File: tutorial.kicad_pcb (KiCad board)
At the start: 2 copper layers, 175 x 164.8 mm, 68 parts

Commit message: define pins
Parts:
- removed the _1 at (246.1, 152.0) (x2)
- added _1 (x2): RPi_Pico_SMD_TH, RPi_Pico_SMD_TH, F.Cu at (246.1, 152.0)
- moved B1 13.9 mm to (229.8, 185.4)
- moved B2 13.9 mm to (229.8, 185.4)
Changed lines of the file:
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@@
         (descr "Low-profile SMD Tactile Switch, https://www.e-switch.com/product-catalog/tact/product-lines/tl3342-series-low-profile-smt-tact-switch")
         (tags "SPST Tactile Switch")
-        (at 243.6963463 183.9408894 -15)
+        (at 229.84521529999998 185.405871 -15)
         (fp_text reference "B1" (at 0 0) (layer F.SilkS) hide (effects (font (size 1.27 1.27) (thickness 0.15))))
         (fp_text value "" (at 0 0) (layer F.SilkS) hide (effects (font (size 1.27 1.27) (thickness 0.15))))
@@
         (descr "Low-profile SMD Tactile Switch, https://www.e-switch.com/product-catalog/tact/product-lines/tl3342-series-low-profile-smt-tact-switch")
         (tags "SPST Tactile Switch")
-        (at 243.6963463 183.9408894 -15)
+        (at 229.84521529999998 185.405871 -15)
         (fp_text reference "B2" (at 0 0) (layer F.SilkS) hide (effects (font (size 1.27 1.27) (thickness 0.15))))
         (fp_text value "" (at 0 0) (layer F.SilkS) hide (effects (font (size 1.27 1.27) (thickness 0.15))))

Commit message: ready to start routing
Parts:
- removed the _1 at (246.1, 152.0) (x2)
- added ROT1: , rotary_encoder, F.Cu at (130.6, 92.3)
- added _1 (x2): RPi_Pico_SMD_TH, RPi_Pico_SMD_TH, F.Cu at (246.6, 153.1)
- added _2: , MountingHole_2.2mm_M2_Pad_Via, F.Cu at (243.6, 200.5)
- added _3: , MountingHole_2.2mm_M2_Pad_Via, F.Cu at (186.1, 203.0)
- added _4: , MountingHole_2.2mm_M2_Pad_Via, F.Cu at (197.3, 91.3)
- added _5: , MountingHole_2.2mm_M2_Pad_Via, F.Cu at (143.0, 84.7)
- moved B1 2.83 mm to (229.3, 188.2), turned to -16 degrees
- moved B2 2.83 mm to (229.3, 188.2), turned to -16 degrees
- moved TRRS1 2.06 mm to (250.4, 194.2), turned to -106 degrees
- moved S28 1.42 mm to (230.1, 120.2), turned to -16 degrees
- moved D28 1.34 mm to (228.7, 125.0), turned to -16 degrees
- moved S27 1.11 mm to (224.7, 138.7), turned to -16 degrees
- moved OLED1 1.11 mm to (244.8, 181.2), turned to -106 degrees
- moved D27 1.04 mm to (223.4, 143.5), turned to -16 degrees
- moved D31 0.95 mm to (221.7, 221.5), turned to -31 degrees
- moved S31 0.93 mm to (224.2, 217.2), turned to -31 degrees
- moved S26 0.83 mm to (219.4, 157.3), turned to -16 degrees
- moved D26 0.76 mm to (218.0, 162.1), turned to -16 degrees
- moved S24 0.75 mm to (211.5, 112.4), turned to -15.5 degrees
- moved S19 0.72 mm to (193.6, 104.8), turned to -15.5 degrees
- moved D24 0.71 mm to (210.1, 117.2), turned to -15.5 degrees
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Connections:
- OLED1 pad 3: GP5 -> GP3
- OLED1 pad 4: GP4 -> GP2
- TRRS1 pad 3: P2 -> GP15
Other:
- board size 175 x 164.8 mm -> 178.2 x 165.7 mm

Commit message: attempt to set up routing
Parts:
- removed the _1 at (246.6, 153.1) (x2)
- added _1 (x2): RPi_Pico_SMD_TH, RPi_Pico_SMD_TH, F.Cu at (246.6, 153.1)
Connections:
- D1 pad 1: (no net) -> GP12
- D10 pad 1: (no net) -> GP13
- D11 pad 1: (no net) -> GP12
- D12 pad 1: (no net) -> GP11
- D13 pad 1: (no net) -> GP10
- D14 pad 1: (no net) -> GP9
- D15 pad 1: (no net) -> GP13
- D16 pad 1: (no net) -> GP12
- D17 pad 1: (no net) -> GP11
- D18 pad 1: (no net) -> GP10
- D19 pad 1: (no net) -> GP9
- D2 pad 1: (no net) -> GP11
- D20 pad 1: (no net) -> GP13
- D21 pad 1: (no net) -> GP12
- D22 pad 1: (no net) -> GP11
- D23 pad 1: (no net) -> GP10
- D24 pad 1: (no net) -> GP9
- D25 pad 1: (no net) -> GP12
- D26 pad 1: (no net) -> GP11
- D27 pad 1: (no net) -> GP10
- D28 pad 1: (no net) -> GP9
- D29 pad 1: (no net) -> GP14
- D3 pad 1: (no net) -> GP10
- D30 pad 1: (no net) -> GP14
- D31 pad 1: (no net) -> GP14
- D4 pad 1: (no net) -> GP9
- D5 pad 1: (no net) -> GP13
- D6 pad 1: (no net) -> GP12
- D7 pad 1: (no net) -> GP11
- D8 pad 1: (no net) -> GP10
- D9 pad 1: (no net) -> GP9
- ROT1 pad 1: GP0 -> GP1
- ROT1 pad 2: GP1 -> GP9
- S1 pad 1: (no net) -> GP1
- S10 pad 1: (no net) -> GP5
- S11 pad 1: (no net) -> GP5
- S12 pad 1: (no net) -> GP5
- S13 pad 1: (no net) -> GP5
- S14 pad 1: (no net) -> GP5
- S15 pad 1: (no net) -> GP6
- S16 pad 1: (no net) -> GP6
- S17 pad 1: (no net) -> GP6
- S18 pad 1: (no net) -> GP6
- S19 pad 1: (no net) -> GP6
- S2 pad 1: (no net) -> GP1
- S20 pad 1: (no net) -> GP7
- S21 pad 1: (no net) -> GP7
- S22 pad 1: (no net) -> GP7
- S23 pad 1: (no net) -> GP7
- S24 pad 1: (no net) -> GP7
- S25 pad 1: (no net) -> GP8
- S26 pad 1: (no net) -> GP8
- S27 pad 1: (no net) -> GP8
- S28 pad 1: (no net) -> GP8
- S29 pad 1: (no net) -> GP8
- S3 pad 1: (no net) -> GP1
- S30 pad 1: (no net) -> GP8
- S31 pad 1: (no net) -> GP8
- S4 pad 1: (no net) -> GP1
- S5 pad 1: (no net) -> GP4
- S6 pad 1: (no net) -> GP4
- S7 pad 1: (no net) -> GP4
- S8 pad 1: (no net) -> GP4
- S9 pad 1: (no net) -> GP4

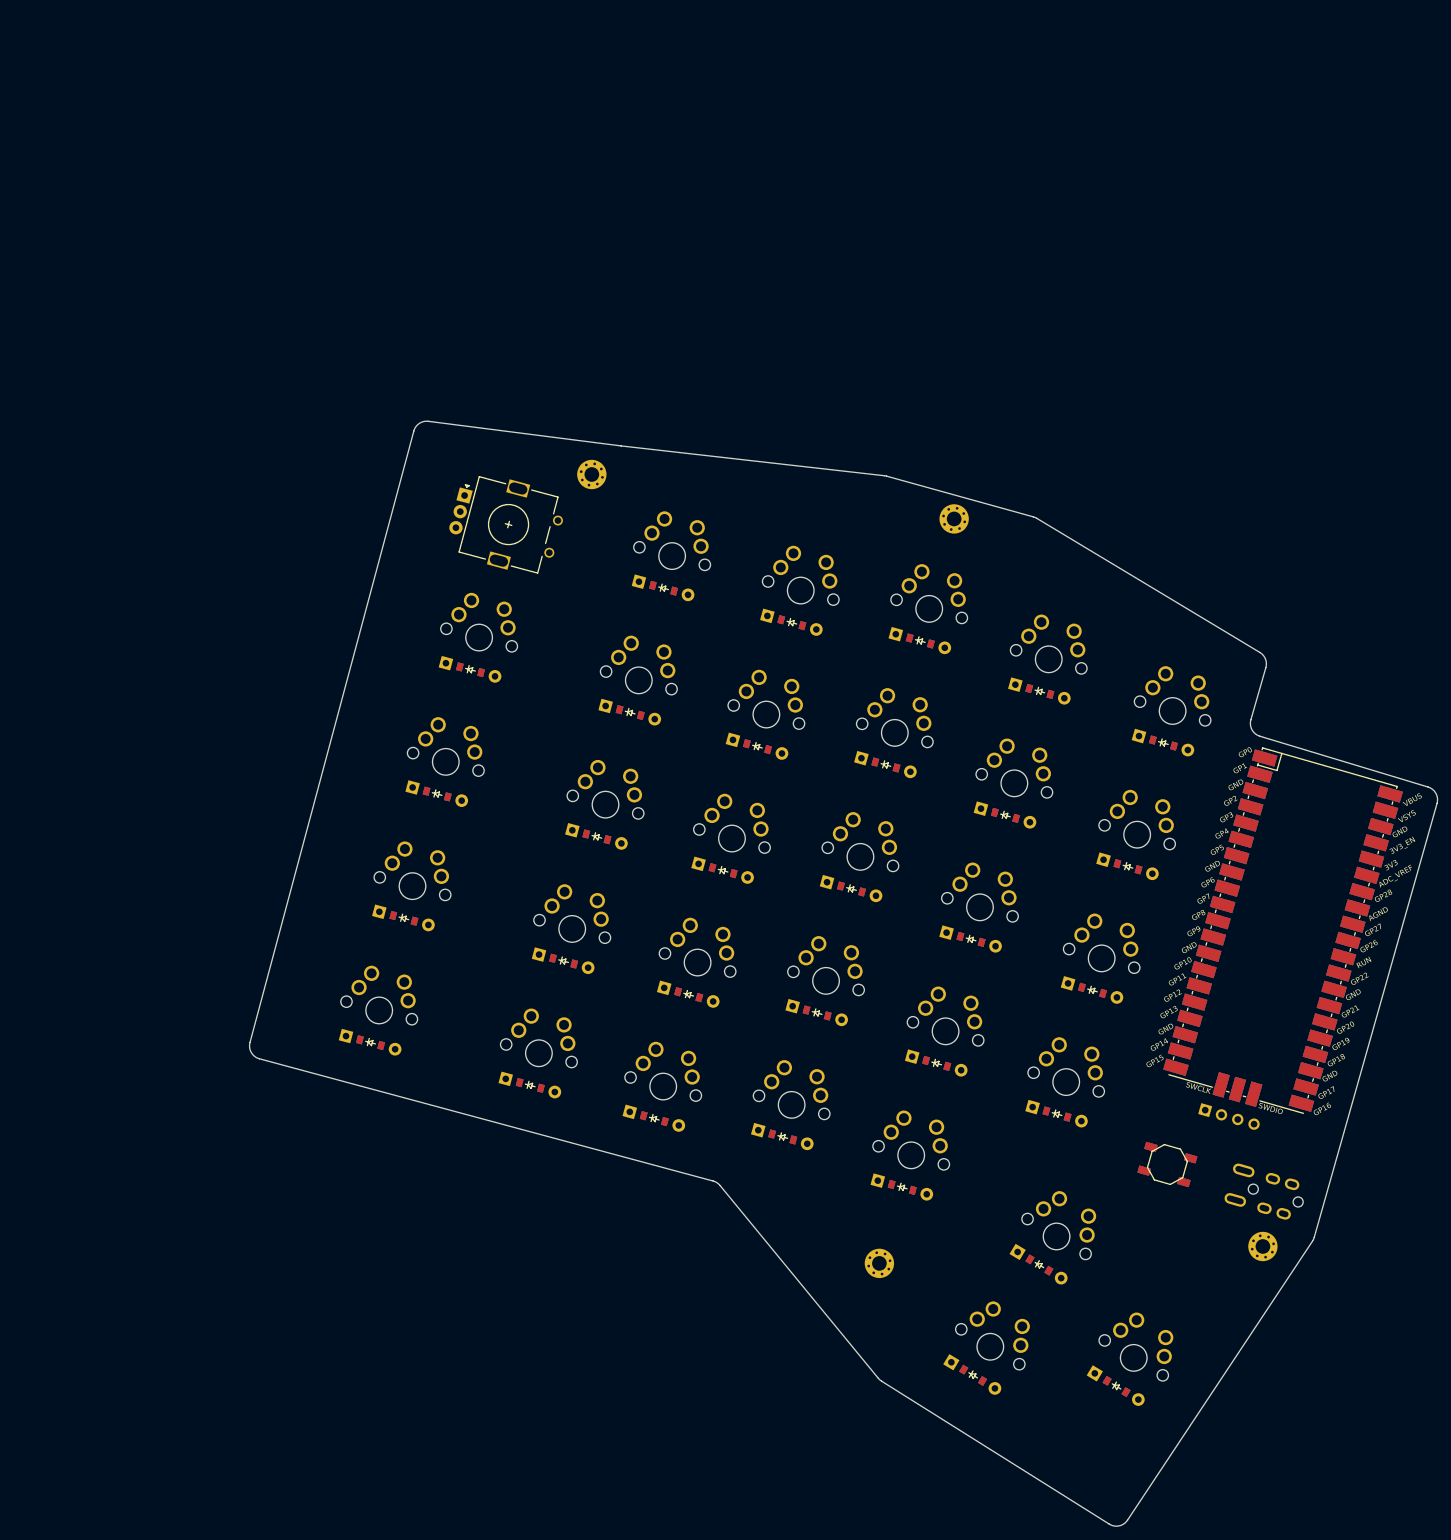
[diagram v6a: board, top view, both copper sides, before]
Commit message: routing setup done, now to actually route
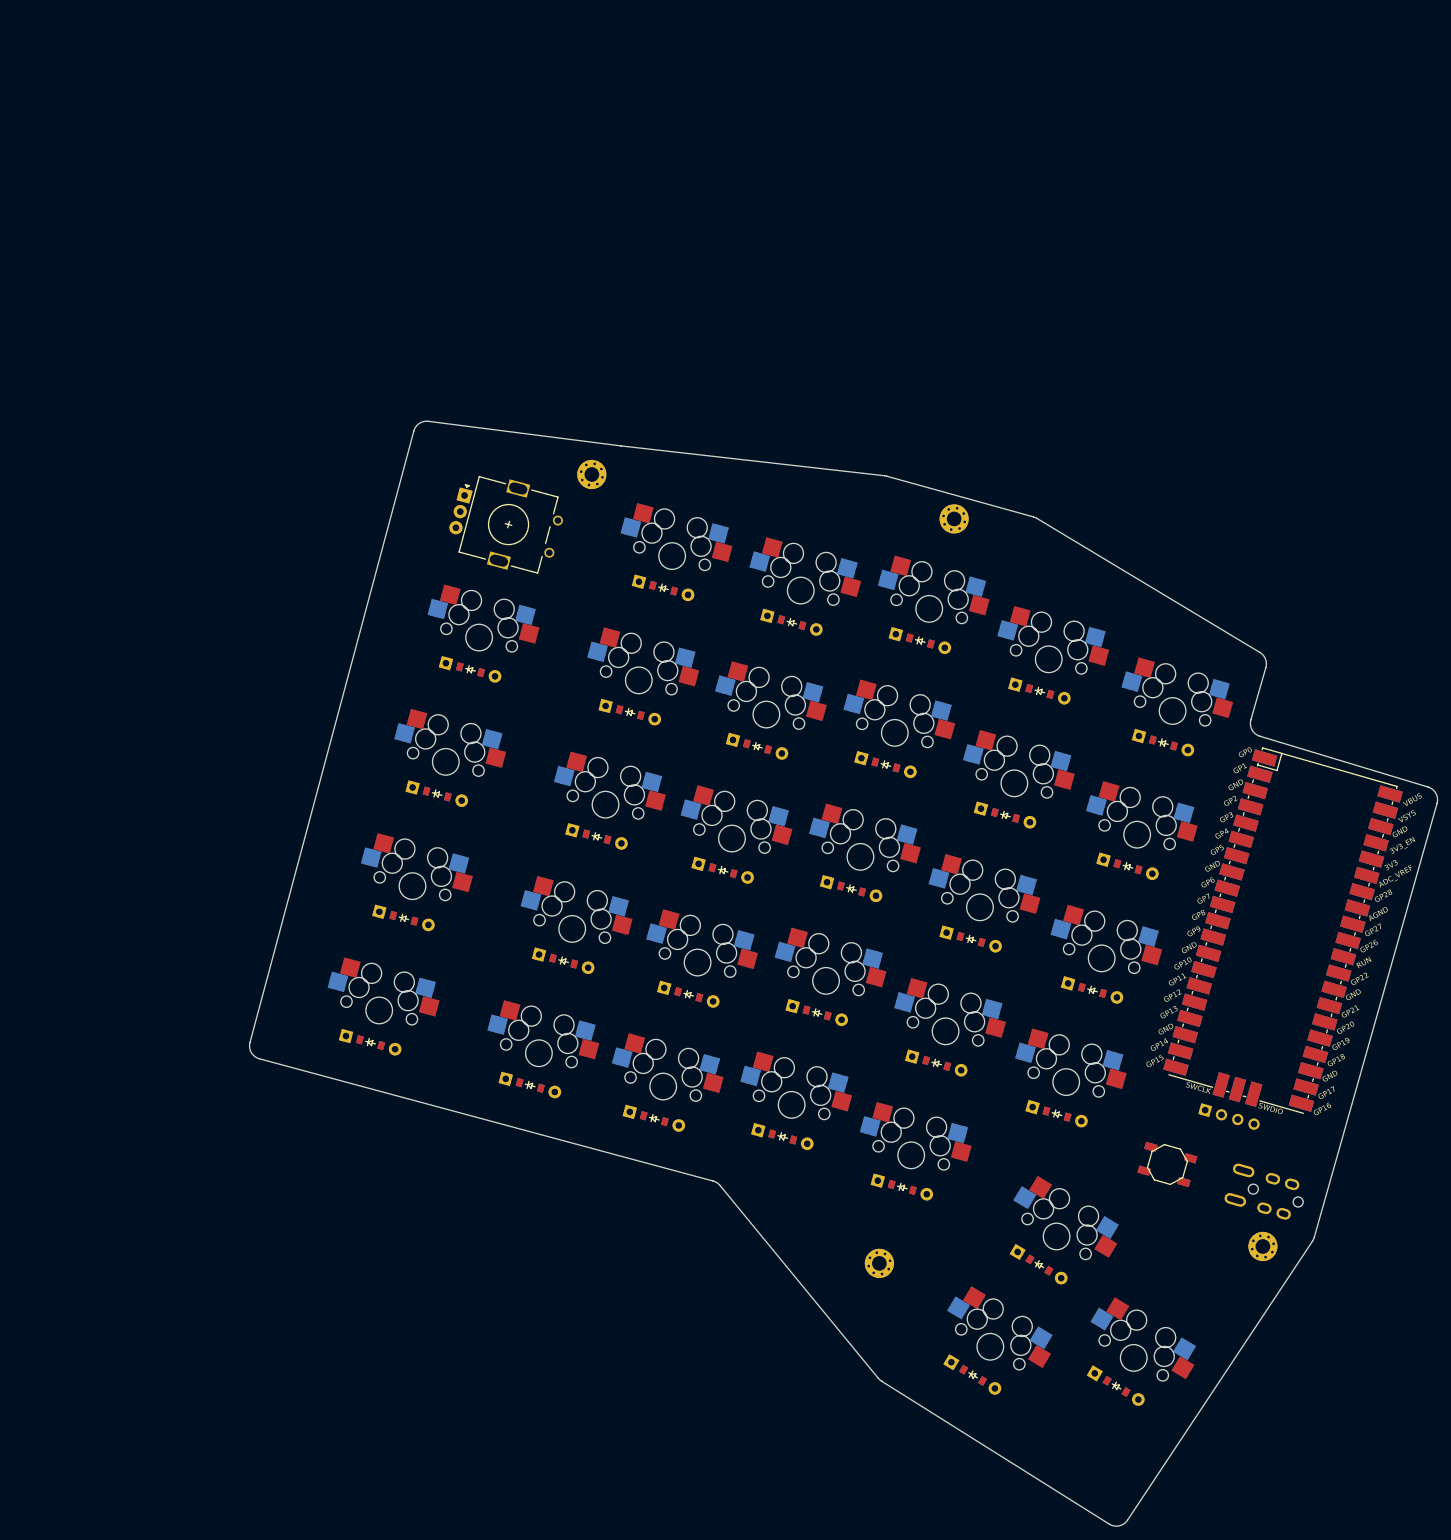
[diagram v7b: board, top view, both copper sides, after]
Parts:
- removed the _1 at (246.6, 153.1) (x2)
- added _1 (x2): RPi_Pico_SMD_TH, RPi_Pico_SMD_TH, F.Cu at (246.6, 153.1)
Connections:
- D30 pad 1: GP14 -> GP13
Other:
- net class Default removed

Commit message: fix routing setup
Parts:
- removed the _1 at (246.6, 153.1) (x2)
- added _1 (x2): RPi_Pico_SMD_TH, RPi_Pico_SMD_TH, F.Cu at (246.6, 153.1)
- turned D1 to 165 degrees
- turned D10 to 164.5 degrees
- turned D11 to 164.5 degrees
- turned D12 to 164.5 degrees
- turned D13 to 164.5 degrees
- turned D14 to 164.5 degrees
- turned D15 to 164.5 degrees
- turned D16 to 164.5 degrees
- turned D17 to 164.5 degrees
- turned D18 to 164.5 degrees
- turned D19 to 164.5 degrees
- turned D2 to 165 degrees
- turned D20 to 164.5 degrees
- turned D21 to 164.5 degrees
- turned D22 to 164.5 degrees
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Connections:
- D1 pad 1: GP12 -> GP13
- D2 pad 1: GP11 -> GP12
- D3 pad 1: GP10 -> GP11
- D4 pad 1: GP9 -> GP10
